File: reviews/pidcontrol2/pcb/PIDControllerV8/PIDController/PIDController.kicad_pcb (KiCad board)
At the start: 2 copper layers, 74.9 x 128.9 mm, 34 parts, among them J1 Conn_02x05_Odd_Even, J3 Screw_Terminal_01x02, J4 Screw_Terminal_01x02, J5 Screw_Terminal_01x02, J6 Screw_Terminal_01x02, J7 Conn_02x03_Odd_Even, U1 Arduino_Nano_33_IoT, U2 TXS0104ED, U3 SN75175D

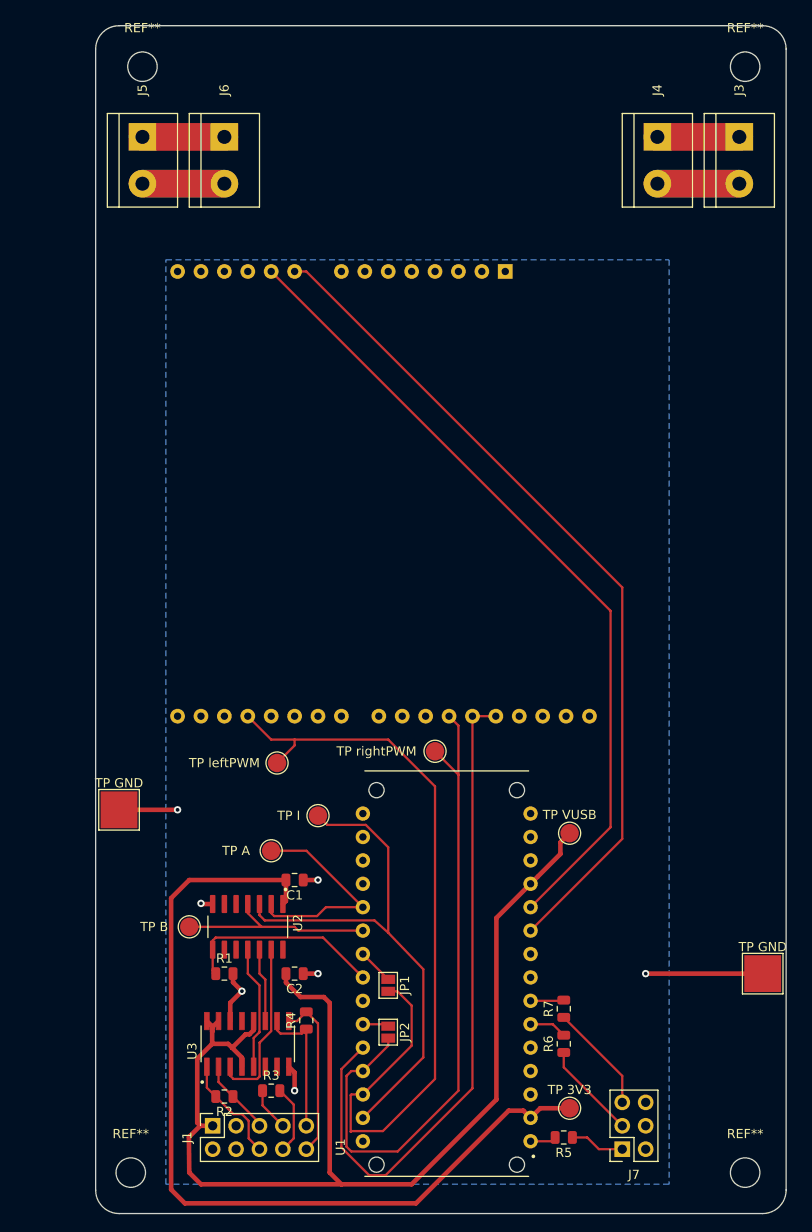
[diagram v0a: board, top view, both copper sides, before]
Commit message: update to PIDControllerv8 and updated review of pidcontrol2.
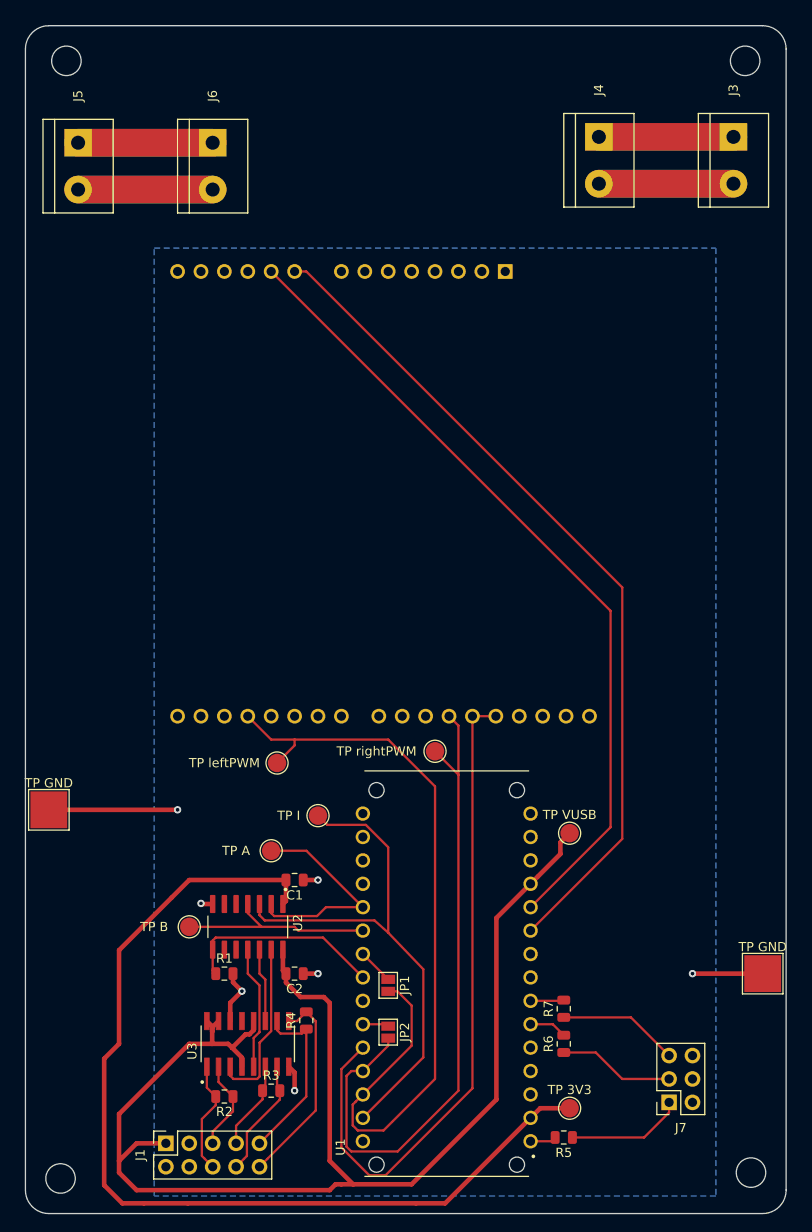
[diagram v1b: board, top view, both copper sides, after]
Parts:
- moved REF** 8.28 mm to (109.9, 31.8)
- moved REF** 7.65 mm to (109.2, 153.0)
- moved TP GND 7.62 mm to (108.0, 113.0)
- moved J7 7.18 mm to (175.3, 144.8)
- moved J5 7.01 mm to (111.1, 40.6)
- moved J4 6.35 mm to (167.6, 40.0)
- moved J1 5.43 mm to (120.7, 149.2)
- moved J6 1.42 mm to (125.7, 40.6)
- moved REF** 0.64 mm to (184.2, 152.4)
- moved REF** 0.63 mm to (183.5, 31.8)
- moved J3 0.63 mm to (182.2, 40.0)
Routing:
- net VUSB: track 126.9 -> 147.2 mm
- net Net-(J3-Pad2): track 17.8 -> 29.2 mm
- net Net-(J3-Pad1): track 17.8 -> 29.2 mm
- net Net-(J5-Pad2): track 17.8 -> 29.2 mm
- net Net-(J5-Pad1): track 17.8 -> 29.2 mm
- net 3V3: track 96.4 -> 105.8 mm
- net Net-(J7-Pad1): track 5.94 -> 12.7 mm
- net ENCODER_NOT_B: track 8.11 -> 13.6 mm
- net ENCODER_B: track 4.94 -> 9.85 mm
- net ENCODER_INDEX: track 15.7 -> 19.7 mm
- net ENCODER_NOT_INDEX: track 18.8 -> 22.6 mm
- net GND: track 32.8 -> 35.3 mm
- net Net-(J7-Pad3): track 10.6 -> 12.6 mm
- net ENCODER_A: track 8.26 -> 9.89 mm
- net leftPWM: track 90.4 -> 88.9 mm
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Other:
- board size 74.9 x 128.9 mm -> 82.6 x 128.9 mm
